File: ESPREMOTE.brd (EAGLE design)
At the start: 47 x 78 mm, 38 parts, among them IC1 ESP12SMT, J1 2.1MM DC Jack, Q1 2N7002, Q2 2N7002, Q3 2N7002, Q4 2N7002

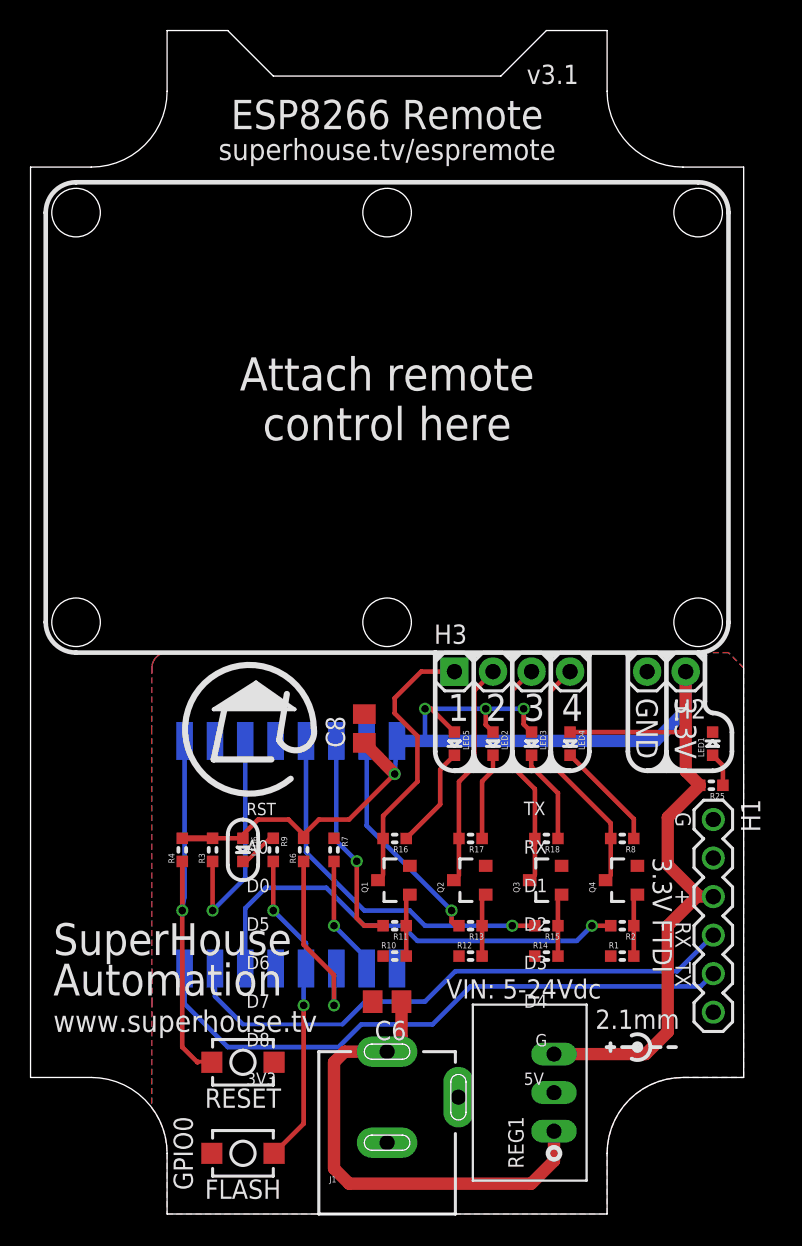
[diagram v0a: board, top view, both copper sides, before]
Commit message: Added reed relays
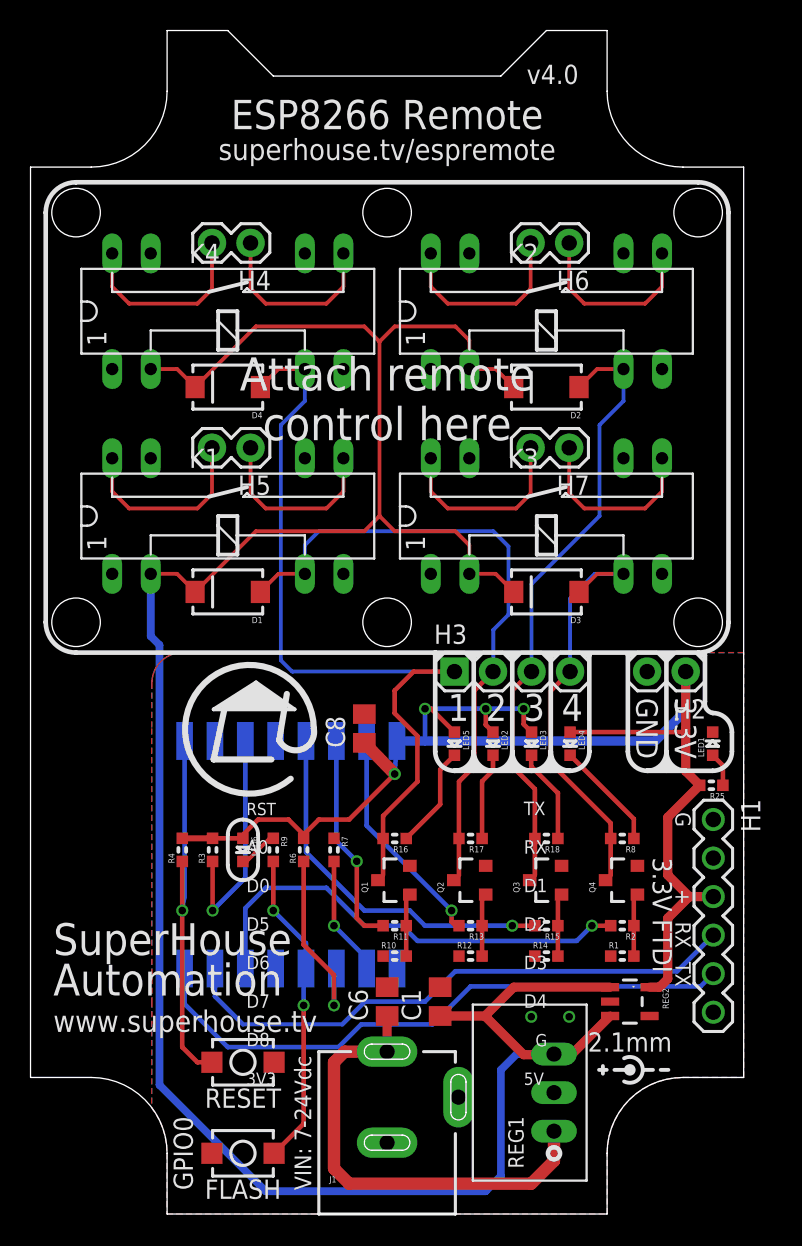
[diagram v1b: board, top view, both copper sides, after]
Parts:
- added C1: 10uF 50V, freetronics-jon:C0805
- added D1, D2, D3, D4: (no value), SparkFun:SMA-DIODE
- added H4, H5, H6, H7: (no value), freetronics-jon:1X02
- added K1, K2, K3, K4: HE751, relay:HE751
- added REG2: AP2112KSOT25, freetronics-jon:SOT23-5
- C6, C8: value 10uF 10V 0805 -> 10uF 50V
- REG1: value K7803-500R3 -> K7805-500R3
- turned C6 to 90 degrees
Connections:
- new net N$12: H4.2, K4.14
- new net N$13: H7.1, K3.8
- new net N$14: H7.2, K3.14
- new net N$8: H4.1, K4.8
- new net OUT1: D4.A, H3.1, K4.6, Q1.3, R16.2
- new net OUT2: D1.A, H3.2, K1.6, Q2.3, R17.2
- new net OUT3: D2.A, H3.3, K2.6, Q3.3, R18.2
- new net OUT4: D3.A, H3.4, K3.6, Q4.3, R8.2
- new net VCC: C6.1, J1.PWR, REG1.1
- net 3.3V: now also REG2.5; no longer REG1.3
- net 5V: now also C1.1, D1.C, D2.C, D3.C, D4.C, K1.2, K2.2, K3.2, K4.2, REG1.3, REG2.1, REG2.3; no longer C6.1, J1.PWR, REG1.1
- net GND: now also C1.2, REG2.2
- net N$3: now also H5.1, K1.8; no longer H3.2, Q2.3, R17.2
- net N$5: now also H5.2, K1.14; no longer H3.1, Q1.3, R16.2
- net N$6: now also H6.1, K2.8; no longer H3.4, Q4.3, R8.2
- net N$9: now also H6.2, K2.14; no longer H3.3, Q3.3, R18.2
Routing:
- net 5V: track 32.0 -> 163.9 mm
- net OUT1: track 0.00 -> 53.7 mm
- net OUT2: track 0.00 -> 43.0 mm
- net OUT3: track 0.00 -> 41.0 mm
- net VCC: track 0.00 -> 30.6 mm
- net OUT4: track 0.00 -> 28.5 mm
- net N$14: track 0.00 -> 12.7 mm
- net N$12: track 0.00 -> 12.7 mm
- net N$8: track 0.00 -> 12.2 mm
- net N$13: track 0.00 -> 12.2 mm
- net 3.3V: track 102.9 -> 92.8 mm
- net N$5: track 18.4 -> 12.7 mm
- net N$6: track 16.1 -> 12.2 mm
- net N$3: track 14.8 -> 12.2 mm
- net N$9: track 15.0 -> 12.7 mm
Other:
- board text added: "VIN: 7-24Vdc"
- board text added: "v4.0"
- board text removed: "VIN: 5-24Vdc"
- board text removed: "v3.1"
